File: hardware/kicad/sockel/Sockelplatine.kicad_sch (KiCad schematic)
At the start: 12 parts, among them J1 24V Eingang, J2 Stapelstecker 2x20, J3 Kettenstecker, Stift (treibt 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, J4 Leistungsstecker, Stift (24V 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, U1 Raspberry Pi Pico, U2 K7805-2000R3

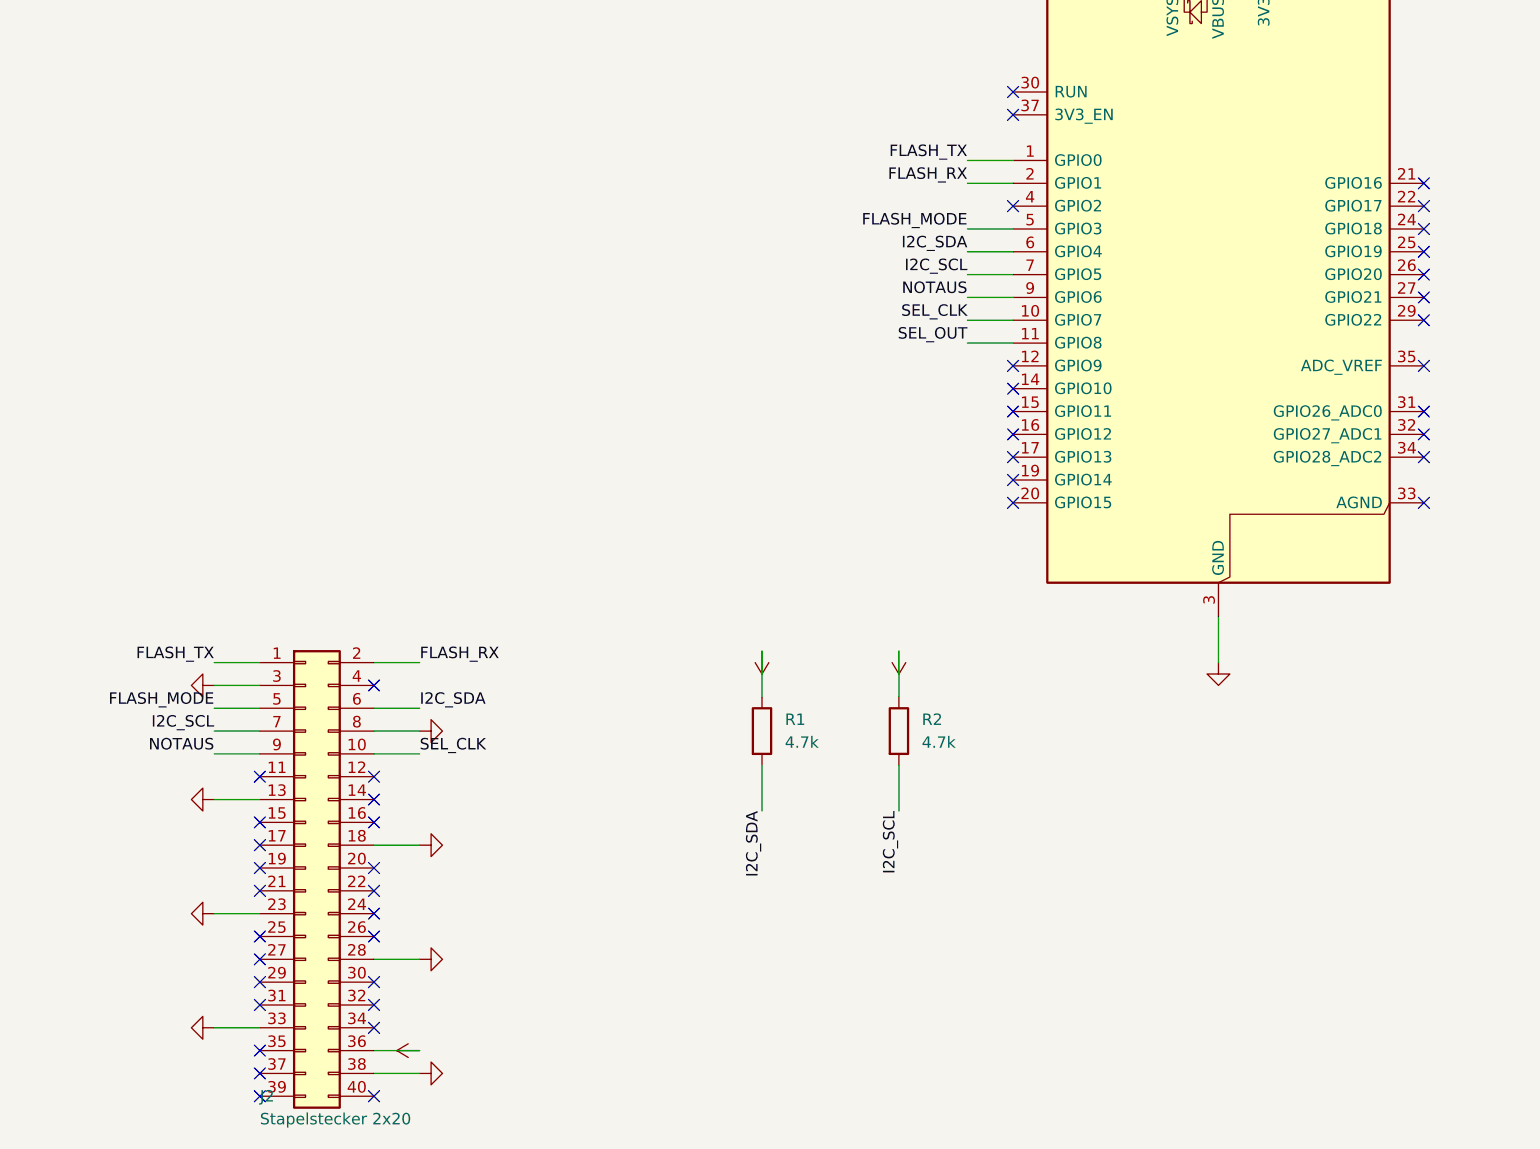
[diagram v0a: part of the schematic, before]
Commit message: Sockelplatine: freie GPIO voll zum Stapel durchreichen, SEL_OUT auf Pin 4 zurueckverlegt
Zwei zusammenhaengende Befunde der vorigen Runde (Aufgabe 4) behoben:

1. Freie Pico-GPIO waren sowohl auf der Sockelplatine (U1) als auch auf
   J2 (modulsockel._stapelstecker()) no_connect -- der Stapelstecker
   leitet zwar mechanisch durch, aber ohne Draht vom Pico dorthin hing
   an keinem freien GPIO je etwas. modulsockel._stapelstecker() bekommt
   dafuer einen neuen Parameter frei_durchreichen (Vorgabe False, jedes
   Modul-J100 unveraendert); die Sockelplatine ruft J2 damit auf und
   verdrahtet U1 unter denselben Netznamen (modulsockel.PIN_GPIO_NAME).
   RUN (Pin 30) und ADC_VREF (Pin 35) bleiben bewusst aussen vor -- kein
   echtes GPIO, RUN ist der aktiv-LOW Reset-Eingang des RP2040.

2. Nach Fix 1 wurde Pin 11 (GP8), bisher lokaler SEL-Treiber ohne
   Vertragsrolle, zu einem durchgereichten freien GPIO -- Kollision mit
   einem Modul, das GP8 selbst nutzt. SEL_OUT bekommt deshalb wieder
   Pin 4 (GP2), wie vor der Steckertrennung: neue Vertragsrolle in
   stack_spec.PIN_ROLLE/RESERVIERT, aber weiterhin kein Pin des 2x20-
   Stapelsteckers (_stapelstecker() behandelt die Rolle explizit als
   no_connect).

Ausserdem: AGND-Kommentar benennt die Abweichung vom Vertrag jetzt
ausdruecklich als solche und zitiert das Pico-Datenblatt (AGND ist laut
Datenblatt keine interne GND-Verbindung, sondern optional verbindbar);
neue Layout-Auflage in hardware/bauteile-1b.md (C3 muss nah an U2 Pin 1
sitzen, sonst untergraebt die Schleifeninduktivitaet die Stuetzwirkung).

Zwei neue Testzusicherungen in tests/test_sockelplatine.py fangen genau
diese beiden Befunde kuenftig ab; beide nachweislich rot, wenn man den
jeweiligen Fehler testweise wieder einbaut. ERC weiterhin 0 Fehler, 1
Warnung (unveraendert lib_symbol_mismatch).

Co-Authored-By: Claude Opus 5 (1M context) <noreply@anthropic.com>
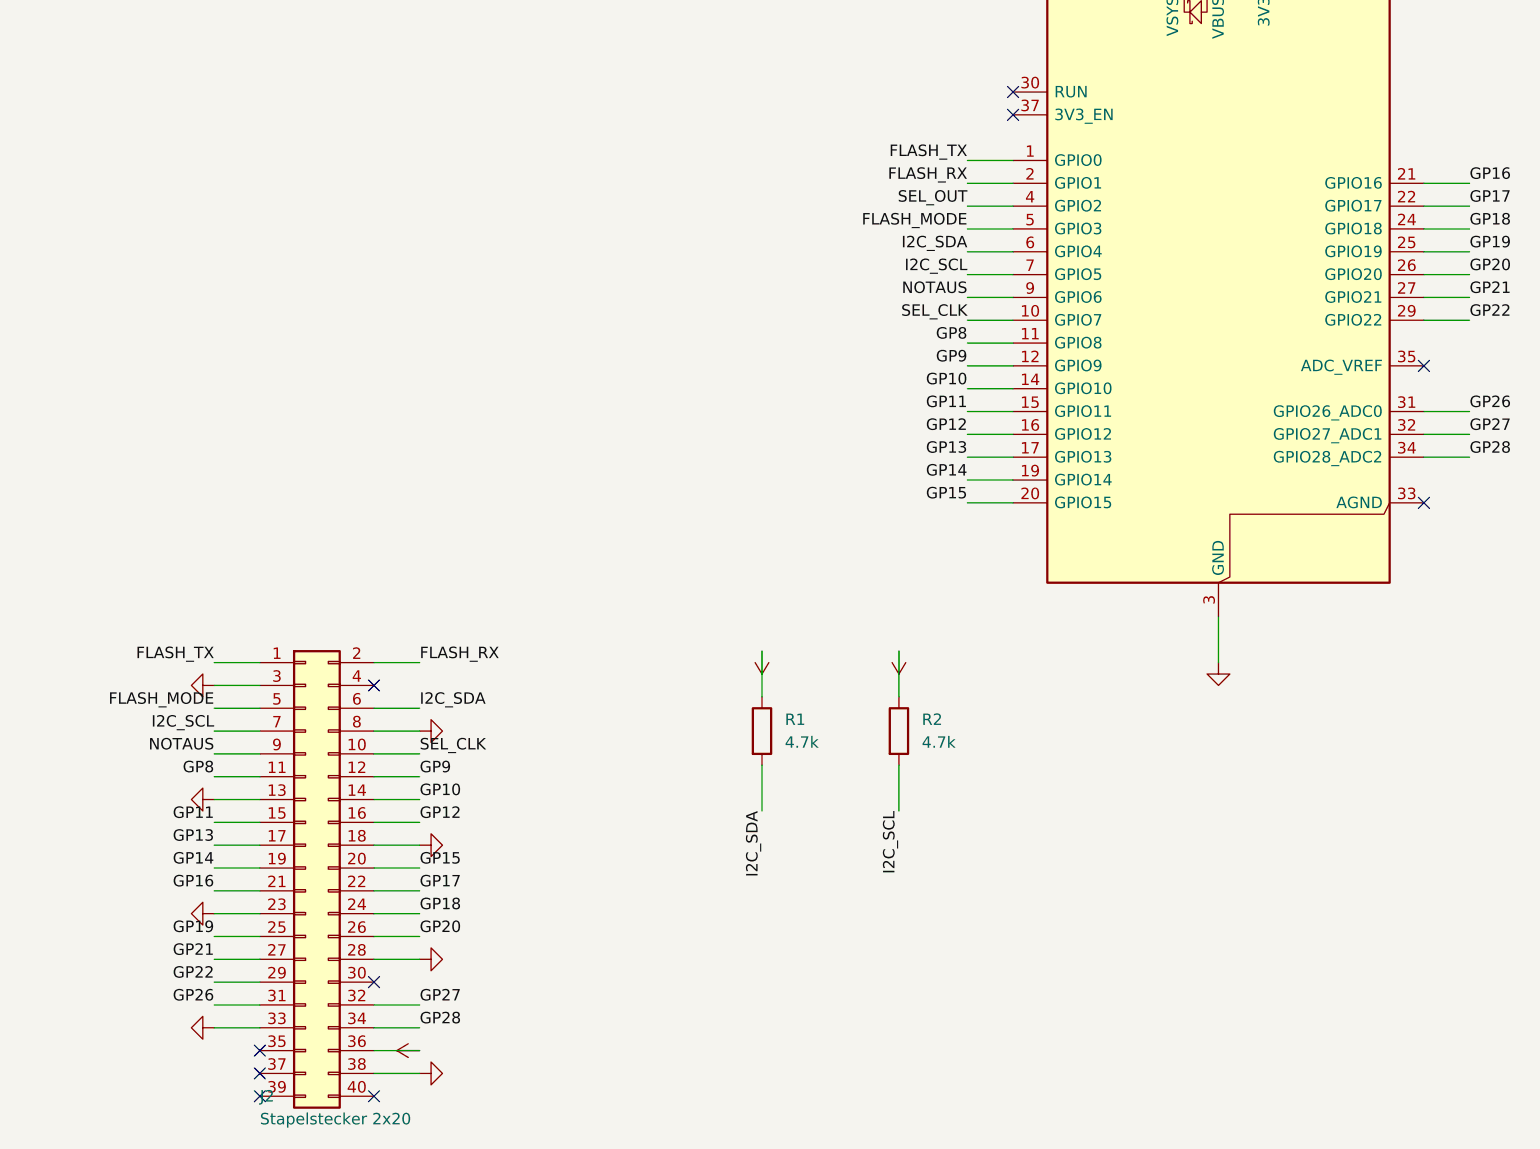
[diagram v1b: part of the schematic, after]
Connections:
- net SEL_OUT: now also U1.4 (GPIO2); no longer U1.11 (GPIO8)
- net GP9: now reaches U1.12 (GPIO9)
- net GP9: now also J2.12 (Pin_12)
- net GP10: now reaches U1.14 (GPIO10)
- net GP10: now also J2.14 (Pin_14)
- net GP11: now reaches U1.15 (GPIO11)
- net GP11: now also J2.15 (Pin_15)
- net GP12: now reaches U1.16 (GPIO12)
- net GP12: now also J2.16 (Pin_16)
- net GP13: now reaches U1.17 (GPIO13)
- net GP13: now also J2.17 (Pin_17)
- net GP14: now reaches U1.19 (GPIO14)
- net GP14: now also J2.19 (Pin_19)
- net GP15: now reaches U1.20 (GPIO15)
- net GP15: now also J2.20 (Pin_20)
- net GP16: now reaches U1.21 (GPIO16)
- net GP16: now also J2.21 (Pin_21)
- net GP17: now reaches U1.22 (GPIO17)
- net GP17: now also J2.22 (Pin_22)
- net GP18: now reaches U1.24 (GPIO18)
- net GP18: now also J2.24 (Pin_24)
- net GP19: now reaches U1.25 (GPIO19)
- net GP19: now also J2.25 (Pin_25)
- net GP20: now reaches U1.26 (GPIO20)
- net GP20: now also J2.26 (Pin_26)
- net GP21: now reaches U1.27 (GPIO21)
- net GP21: now also J2.27 (Pin_27)
- net GP22: now reaches U1.29 (GPIO22)
- net GP22: now also J2.29 (Pin_29)
- net GP26: now reaches U1.31 (GPIO26_ADC0)
- net GP26: now also J2.31 (Pin_31)
- net GP27: now reaches U1.32 (GPIO27_ADC1)
- net GP27: now also J2.32 (Pin_32)
- net GP28: now reaches U1.34 (GPIO28_ADC2)
- net GP28: now also J2.34 (Pin_34)
- net GP8: now reaches J2.11 (Pin_11)
- net GP8: now also U1.11 (GPIO8)
- no-connect marks 47 -> 11

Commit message: Der eingecheckte Sockelschaltplan war nicht der Stand seines Generators
J3/J4 trugen noch die bedrahteten Steckerfootprints. Auf SMD-Paare
umgestellt wurde in fa46a9f (Aufgabe 5e); der Sockelschaltplan wurde
zuletzt in 15fa36d erzeugt, also davor. Der Generator war die ganze
Zeit richtig, nur nie wieder gelaufen. Das Motormodul war zufaellig
in Ordnung -- es wurde nach fa46a9f noch einmal erzeugt.

Aufgabe 6 haette daraus bedrahtete Stecker an SMD-Koordinaten gesetzt:
STECKER_POS rechnet mit den SMD-Hoefen, deren Loetpads seitlich neben
den Stiften liegen statt mittig darunter. Aufgefallen waere das erst
an der gefertigten Platine.

Kein bestehendes Gate konnte das sehen -- nachgemessen, nicht vermutet:
mit der veralteten Datei liefen alle sieben Testreihen gruen und ERC
meldete unveraendert 0 Fehler / 1 Warnung. Die Testreihen pruefen den
Generator gegen den Vertrag und sehen sein Erzeugnis nie an; ERC prueft
Verbindungen, und die waren richtig -- nur das Bauteil darunter war ein
anderes.

Als Klasse geschlossen, nicht als Einzelfall: beide Generatoren geben
ihre Erzeugungsangaben jetzt als Modulkonstanten frei und bauen ueber
erzeugen(ziel), damit der neue Test dieselbe Funktion aufruft statt
Projektname und Datum abzuschreiben. tests/test_erzeugte_dateien.py
haelt jede eingecheckte .kicad_sch gegen einen frischen Lauf ihres
Generators (Blatt-Kennungen vereinheitlicht -- sie sind je Lauf
zufaellig und waren beim Sockel 72 der 80 geaenderten Zeilen).
Rot-Probe: mit der alten Datei nennt der Test die vier abweichenden
Zeilen von J3/J4 und den Befehl, der sie behebt.

Co-Authored-By: Claude Opus 5 (1M context) <noreply@anthropic.com>
Claude-Session: https://claude.ai/code/session_01KDus95JJwCeRuwccgBWEi5
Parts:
- J3: value Kettenstecker, Stift (treibt SEL) -> Kettenstecker, Stift SMD (treibt SEL); footprint Connector_PinHeader_2.54mm:PinHeader_1x02_P2.54mm_Vertical -> Connector_PinHeader_2.54mm:PinHeader_1x02_P2.54mm_Vertical_SMD_Pin1Left
- J4: value Leistungsstecker, Stift (24V in den Stapel) -> Leistungsstecker, Stift SMD (24V in den Stapel); footprint Connector_PinHeader_2.54mm:PinHeader_2x02_P2.54mm_Vertical -> Connector_PinHeader_2.54mm:PinHeader_2x02_P2.54mm_Vertical_SMD
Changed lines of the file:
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@@
 		(instances
 			(project "Sockelplatine"
-				(path "/b785d1aa-922b-4be8-9d3e-77c3548b9f40"
+				(path "/c061e268-1aba-4406-8e69-b69d34927629"
 					(reference "J1")
 					(unit 1)
@@
 		(instances
 			(project "Sockelplatine"
-				(path "/b785d1aa-922b-4be8-9d3e-77c3548b9f40"
+				(path "/c061e268-1aba-4406-8e69-b69d34927629"
 					(reference "#FLG1")
 					(unit 1)
@@
 		(instances
 			(project "Sockelplatine"
-				(path "/b785d1aa-922b-4be8-9d3e-77c3548b9f40"
+				(path "/c061e268-1aba-4406-8e69-b69d34927629"
 					(reference "D1")
 					(unit 1)
@@
 		(instances
 			(project "Sockelplatine"
-				(path "/b785d1aa-922b-4be8-9d3e-77c3548b9f40"
+				(path "/c061e268-1aba-4406-8e69-b69d34927629"
 					(reference "C3")
 					(unit 1)
@@
 		(instances
 			(project "Sockelplatine"
-				(path "/b785d1aa-922b-4be8-9d3e-77c3548b9f40"
+				(path "/c061e268-1aba-4406-8e69-b69d34927629"
 					(reference "C1")
 					(unit 1)
@@
 		(instances
 			(project "Sockelplatine"
-				(path "/b785d1aa-922b-4be8-9d3e-77c3548b9f40"
+				(path "/c061e268-1aba-4406-8e69-b69d34927629"
 					(reference "U2")
 					(unit 1)
@@
 		(instances
 			(project "Sockelplatine"
-				(path "/b785d1aa-922b-4be8-9d3e-77c3548b9f40"
+				(path "/c061e268-1aba-4406-8e69-b69d34927629"
 					(reference "C2")
 					(unit 1)
@@
 			)
 		)
-		(property "Value" "Leistungsstecker, Stift (24V in den Stapel)"
+		(property "Value" "Leistungsstecker, Stift SMD (24V in den Stapel)"
 			(at 15.24 -26.67 0)
 			(show_name no)
@@
 			)
 		)
-		(property "Footprint" "Connector_PinHeader_2.54mm:PinHeader_2x02_P2.54mm_Vertical"
+		(property "Footprint" "Connector_PinHeader_2.54mm:PinHeader_2x02_P2.54mm_Vertical_SMD"
 			(at 20.32 -33.02 0)
 			(show_name no)
@@
 		(instances
 			(project "Sockelplatine"
-				(path "/b785d1aa-922b-4be8-9d3e-77c3548b9f40"
+				(path "/c061e268-1aba-4406-8e69-b69d34927629"
 					(reference "J4")
 					(unit 1)
@@
 			)
 		)
-		(property "Value" "Kettenstecker, Stift (treibt SEL)"
+		(property "Value" "Kettenstecker, Stift SMD (treibt SEL)"
 			(at 71.12 -49.53 0)
 			(show_name no)
@@
 			)
 		)
-		(property "Footprint" "Connector_PinHeader_2.54mm:PinHeader_1x02_P2.54mm_Vertical"
+		(property "Footprint" "Connector_PinHeader_2.54mm:PinHeader_1x02_P2.54mm_Vertical_SMD_Pin1Left"
 			(at 76.2 -55.88 0)
 			(show_name no)
@@
 		(instances
 			(project "Sockelplatine"
-				(path "/b785d1aa-922b-4be8-9d3e-77c3548b9f40"
+				(path "/c061e268-1aba-4406-8e69-b69d34927629"
 					(reference "J3")
 					(unit 1)
@@
 		(instances
 			(project "Sockelplatine"
-				(path "/b785d1aa-922b-4be8-9d3e-77c3548b9f40"
+				(path "/c061e268-1aba-4406-8e69-b69d34927629"
 					(reference "J2")
 					(unit 1)
@@
 		(instances
 			(project "Sockelplatine"
-				(path "/b785d1aa-922b-4be8-9d3e-77c3548b9f40"
+				(path "/c061e268-1aba-4406-8e69-b69d34927629"
 					(reference "U1")
 					(unit 1)
@@
 		(instances
 			(project "Sockelplatine"
-				(path "/b785d1aa-922b-4be8-9d3e-77c3548b9f40"
+				(path "/c061e268-1aba-4406-8e69-b69d34927629"
 					(reference "R1")
 					(unit 1)
@@
 		(instances
 			(project "Sockelplatine"
-				(path "/b785d1aa-922b-4be8-9d3e-77c3548b9f40"
+				(path "/c061e268-1aba-4406-8e69-b69d34927629"
 					(reference "R2")
 					(unit 1)
@@
 		(instances
 			(project "Sockelplatine"
-				(path "/b785d1aa-922b-4be8-9d3e-77c3548b9f40"
+				(path "/c061e268-1aba-4406-8e69-b69d34927629"
 					(reference "#PWR177")
 					(unit 1)
@@
 		(instances
 			(project "Sockelplatine"
-				(path "/b785d1aa-922b-4be8-9d3e-77c3548b9f40"
+				(path "/c061e268-1aba-4406-8e69-b69d34927629"
 					(reference "#PWR179")
 					(unit 1)
@@
 		(instances
 			(project "Sockelplatine"
-				(path "/b785d1aa-922b-4be8-9d3e-77c3548b9f40"
+				(path "/c061e268-1aba-4406-8e69-b69d34927629"
 					(reference "#PWR181")
 					(unit 1)
@@
 		(instances
 			(project "Sockelplatine"
-				(path "/b785d1aa-922b-4be8-9d3e-77c3548b9f40"
+				(path "/c061e268-1aba-4406-8e69-b69d34927629"
 					(reference "#PWR183")
 					(unit 1)
@@
 		(instances
 			(project "Sockelplatine"
-				(path "/b785d1aa-922b-4be8-9d3e-77c3548b9f40"
+				(path "/c061e268-1aba-4406-8e69-b69d34927629"
 					(reference "#PWR185")
 					(unit 1)
@@
 		(instances
 			(project "Sockelplatine"
-				(path "/b785d1aa-922b-4be8-9d3e-77c3548b9f40"
+				(path "/c061e268-1aba-4406-8e69-b69d34927629"
 					(reference "#PWR187")
 					(unit 1)
@@
 		(instances
 			(project "Sockelplatine"
-				(path "/b785d1aa-922b-4be8-9d3e-77c3548b9f40"
+				(path "/c061e268-1aba-4406-8e69-b69d34927629"
 					(reference "#PWR189")
 					(unit 1)
@@
 		(instances
 			(project "Sockelplatine"
-				(path "/b785d1aa-922b-4be8-9d3e-77c3548b9f40"
+				(path "/c061e268-1aba-4406-8e69-b69d34927629"
 					(reference "#PWR191")
 					(unit 1)
@@
 		(instances
 			(project "Sockelplatine"
-				(path "/b785d1aa-922b-4be8-9d3e-77c3548b9f40"
+				(path "/c061e268-1aba-4406-8e69-b69d34927629"
 					(reference "#PWR193")
 					(unit 1)
@@
 		(instances
 			(project "Sockelplatine"
-				(path "/b785d1aa-922b-4be8-9d3e-77c3548b9f40"
+				(path "/c061e268-1aba-4406-8e69-b69d34927629"
 					(reference "#PWR195")
 					(unit 1)
@@
 		(instances
 			(project "Sockelplatine"
-				(path "/b785d1aa-922b-4be8-9d3e-77c3548b9f40"
+				(path "/c061e268-1aba-4406-8e69-b69d34927629"
 					(reference "#PWR197")
 					(unit 1)
@@
 		(instances
 			(project "Sockelplatine"
-				(path "/b785d1aa-922b-4be8-9d3e-77c3548b9f40"
+				(path "/c061e268-1aba-4406-8e69-b69d34927629"
 					(reference "#PWR199")
 					(unit 1)
@@
 		(instances
 			(project "Sockelplatine"
-				(path "/b785d1aa-922b-4be8-9d3e-77c3548b9f40"
+				(path "/c061e268-1aba-4406-8e69-b69d34927629"
 					(reference "#PWR201")
 					(unit 1)
@@
 		(instances
 			(project "Sockelplatine"
-				(path "/b785d1aa-922b-4be8-9d3e-77c3548b9f40"
+				(path "/c061e268-1aba-4406-8e69-b69d34927629"
 					(reference "#PWR203")
 					(unit 1)
@@
 		(instances
 			(project "Sockelplatine"
-				(path "/b785d1aa-922b-4be8-9d3e-77c3548b9f40"
+				(path "/c061e268-1aba-4406-8e69-b69d34927629"
 					(reference "#PWR205")
 					(unit 1)
@@
 		(instances
 			(project "Sockelplatine"
-				(path "/b785d1aa-922b-4be8-9d3e-77c3548b9f40"
+				(path "/c061e268-1aba-4406-8e69-b69d34927629"
 					(reference "#PWR207")
 					(unit 1)
@@
 		(instances
 			(project "Sockelplatine"
-				(path "/b785d1aa-922b-4be8-9d3e-77c3548b9f40"
+				(path "/c061e268-1aba-4406-8e69-b69d34927629"
 					(reference "#PWR209")
 					(unit 1)
@@
 		(instances
 			(project "Sockelplatine"
-				(path "/b785d1aa-922b-4be8-9d3e-77c3548b9f40"
+				(path "/c061e268-1aba-4406-8e69-b69d34927629"
 					(reference "#PWR211")
 					(unit 1)
@@
 		(instances
 			(project "Sockelplatine"
-				(path "/b785d1aa-922b-4be8-9d3e-77c3548b9f40"
+				(path "/c061e268-1aba-4406-8e69-b69d34927629"
 					(reference "#PWR213")
 					(unit 1)
@@
 		(instances
 			(project "Sockelplatine"
-				(path "/b785d1aa-922b-4be8-9d3e-77c3548b9f40"
+				(path "/c061e268-1aba-4406-8e69-b69d34927629"
 					(reference "#PWR215")
 					(unit 1)
@@
 		(instances
 			(project "Sockelplatine"
-				(path "/b785d1aa-922b-4be8-9d3e-77c3548b9f40"
+				(path "/c061e268-1aba-4406-8e69-b69d34927629"
 					(reference "#PWR217")
 					(unit 1)
@@
 		(instances
 			(project "Sockelplatine"
-				(path "/b785d1aa-922b-4be8-9d3e-77c3548b9f40"
+				(path "/c061e268-1aba-4406-8e69-b69d34927629"
 					(reference "#PWR219")
 					(unit 1)
